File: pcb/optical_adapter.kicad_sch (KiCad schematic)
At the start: 17 parts, among them J1 Conn_01x06_Pin, Q1 BC847, Q2 BC847, Q3 BC857, Q4 BC817, U1 LM1117MP-3.3

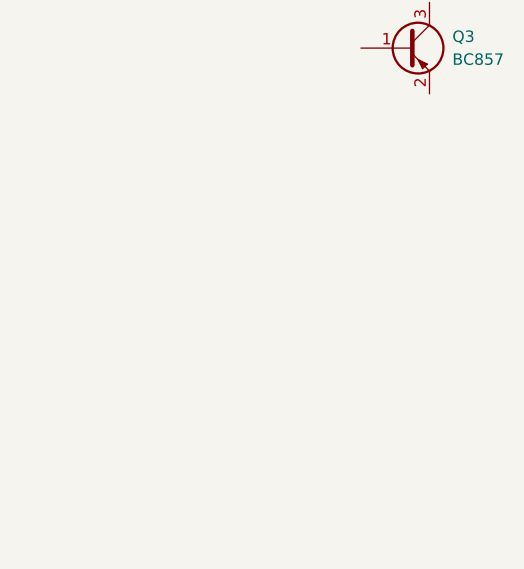
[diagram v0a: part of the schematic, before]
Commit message: Add PCB coil footprint
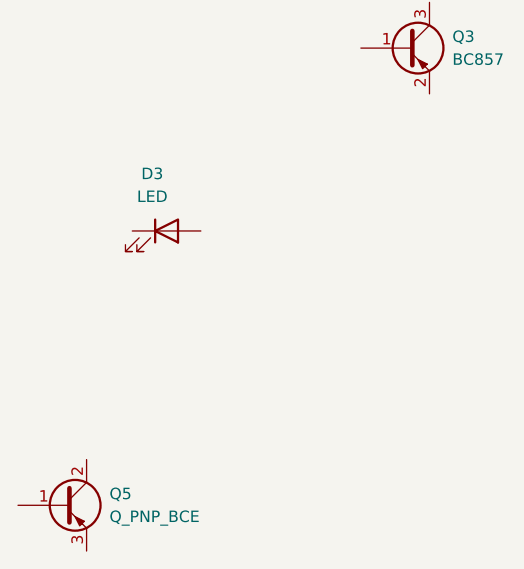
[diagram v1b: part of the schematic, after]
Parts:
- added D3: LED, symbol Device:LED
- added Q5: Q_PNP_BCE, symbol Device:Q_PNP_BCE
- L1: footprint (none) -> footprints:26_turn_16_dia_5_mil
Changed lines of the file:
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@@
 			)
 		)
-		(property "Footprint" ""
+		(property "Footprint" "footprints:26_turn_16_dia_5_mil"
 			(at 106.68 80.01 0)
 			(effects
@@
 			)
 		)
+		(property "LCSC" ""
+			(at 106.68 80.01 0)
+			(effects
+				(font
+					(size 1.27 1.27)
+				)
+				(hide yes)
+			)
+		)
 		(pin "2"
 		)
@@
 	)
 	(symbol
+		(lib_id "Device:LED")
+		(at 50.8 64.77 0)
+		(unit 1)
+		(exclude_from_sim no)
+		(in_bom yes)
+		(on_board yes)
+		(dnp no)
+		(fields_autoplaced yes)
+		(property "Reference" "D3"
+			(at 49.2125 58.42 0)
+			(effects
+				(font
+					(size 1.27 1.27)
+				)
+			)
+		)
+		(property "Value" "LED"
+			(at 49.2125 60.96 0)
+			(effects
+				(font
+					(size 1.27 1.27)
+				)
+			)
+		)
+		(property "Footprint" ""
+			(at 50.8 64.77 0)
+			(effects
+				(font
+					(size 1.27 1.27)
+				)
+				(hide yes)
+			)
+		)
+		(property "Datasheet" "~"
+			(at 50.8 64.77 0)
+			(effects
+				(font
+					(size 1.27 1.27)
+				)
+				(hide yes)
+			)
+		)
+		(property "Description" "Light emitting diode"
+			(at 50.8 64.77 0)
+			(effects
+				(font
+					(size 1.27 1.27)
+				)
+				(hide yes)
+			)
+		)
+		(pin "2"
+		)
+		(pin "1"
+		)
+		(instances
+			(project ""
+				(path "/eed9174b-005f-42ed-94b9-b0e600055621"
+					(reference "D3")
+					(unit 1)
+				)
+			)
+		)
+	)
+	(symbol
 		(lib_id "Jumper:SolderJumper_3_Bridged12")
 		(at 162.56 25.4 0)
@@
 					(unit 1)
 				)
+			)
+		)
+	)
+	(symbol
+		(lib_id "Device:Q_PNP_BCE")
+		(at 39.37 95.25 0)
+		(unit 1)
+		(exclude_from_sim no)
+		(in_bom yes)
+		(on_board yes)
+		(dnp no)
+		(fields_autoplaced yes)
+		(property "Reference" "Q5"
+			(at 44.45 93.9799 0)
+			(effects
+				(font
+					(size 1.27 1.27)
+				)
+				(justify left)
+			)
+		)
+		(property "Value" "Q_PNP_BCE"
+			(at 44.45 96.5199 0)
+			(effects
+				(font
+					(size 1.27 1.27)
+				)
+				(justify left)
+			)
+		)
+		(property "Footprint" ""
+			(at 44.45 92.71 0)
+			(effects
+				(font
+					(size 1.27 1.27)
+				)
+				(hide yes)
+			)
+		)
+		(property "Datasheet" "~"
+			(at 39.37 95.25 0)
+			(effects
+				(font
+					(size 1.27 1.27)
+				)
+				(hide yes)
+			)
+		)
+		(property "Description" "PNP transistor, base/collector/emitter"
+			(at 39.37 95.25 0)
+			(effects
+				(font
+					(size 1.27 1.27)
+				)
+				(hide yes)
+			)
+		)
+		(pin "2"
+		)
+		(pin "1"
+		)
+		(pin "3"
+		)
+		(instances
+			(project ""
+				(path "/eed9174b-005f-42ed-94b9-b0e600055621"
+					(reference "Q5")
+					(unit 1)
+				)

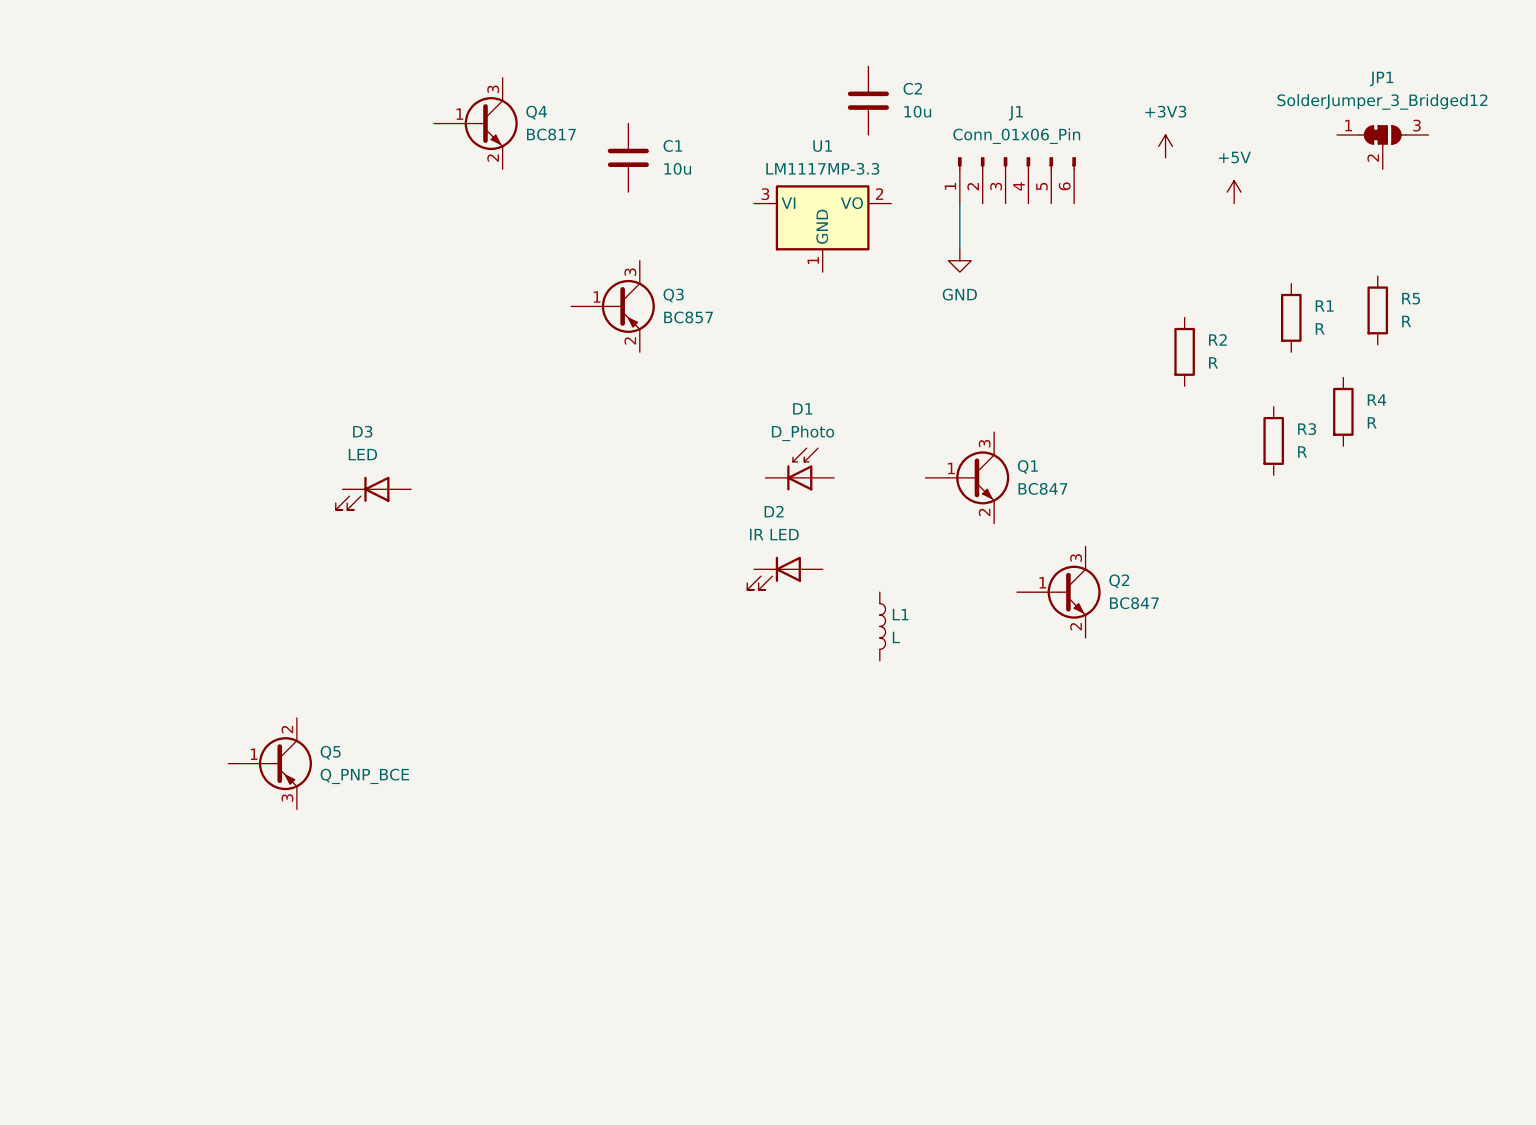
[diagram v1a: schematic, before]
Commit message: Add power supply circuit
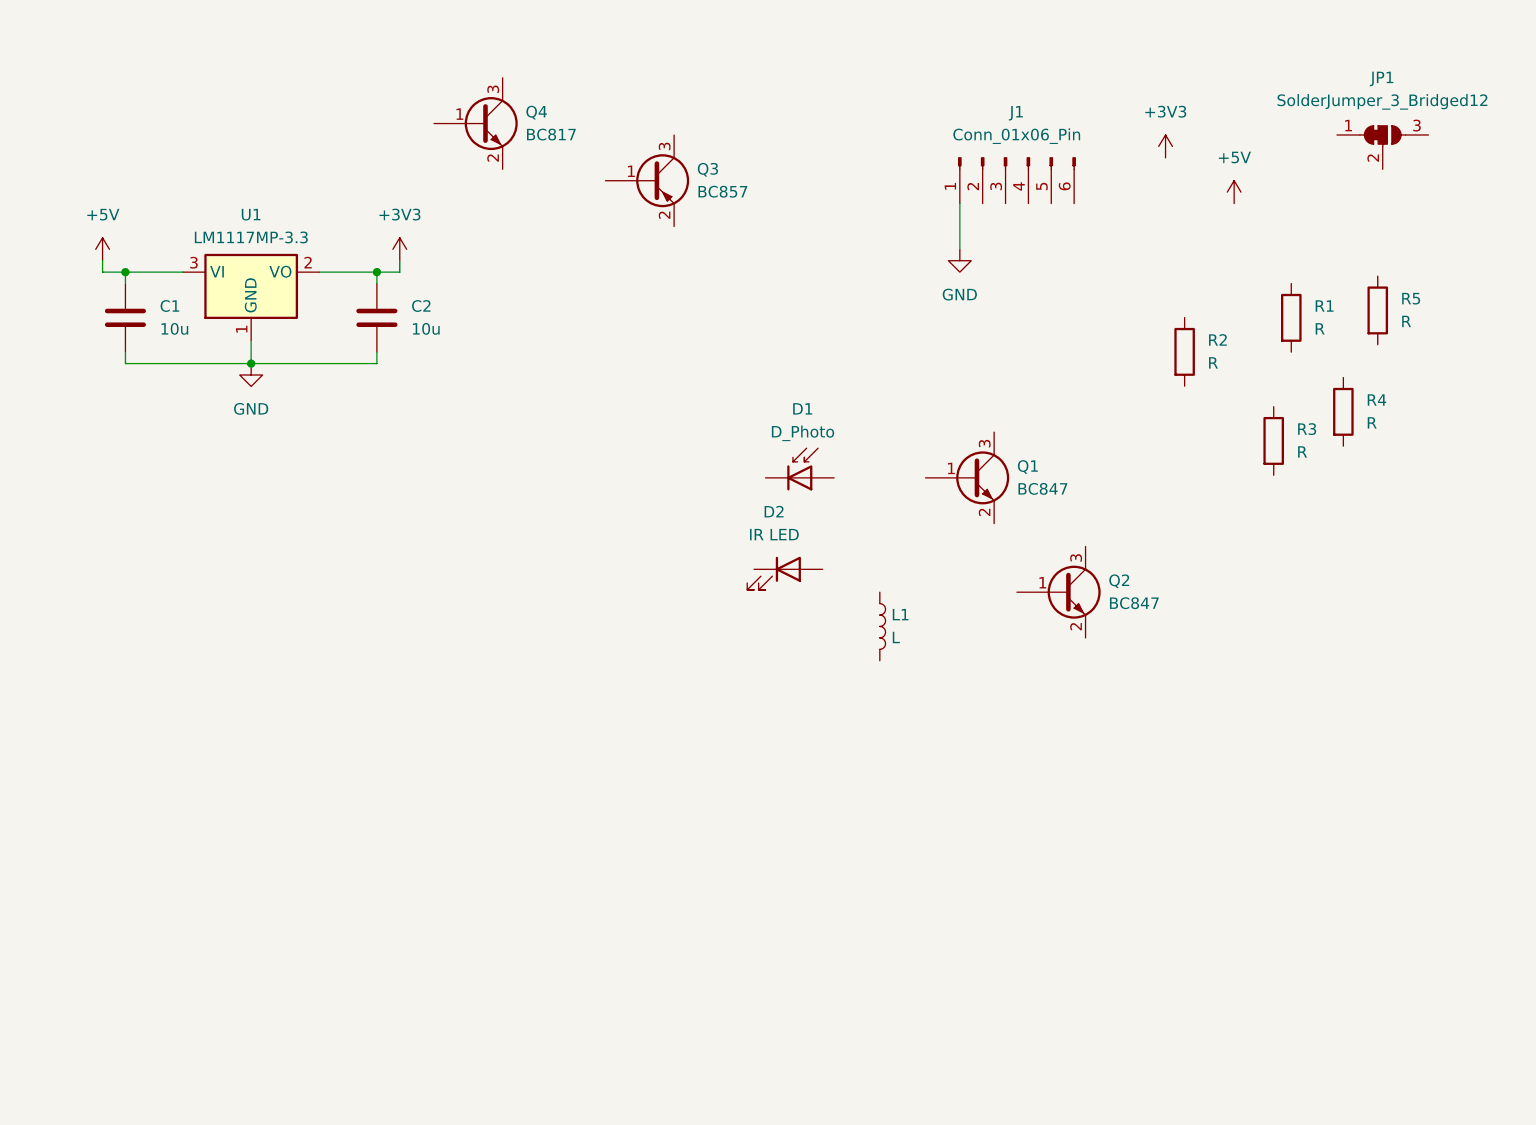
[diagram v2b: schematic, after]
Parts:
- removed D3: LED, symbol Device:LED
- removed Q5: Q_PNP_BCE, symbol Device:Q_PNP_BCE
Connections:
- net +3V3: now also C2.1, U1.2 (VO)
- net +5V: now also C1.1, U1.3 (VI)
- net GND: now also C1.2, C2.2, U1.1 (GND)
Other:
- moved on the sheet: C1, C2, Q3, U1

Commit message: Add IR RX/TX circuit
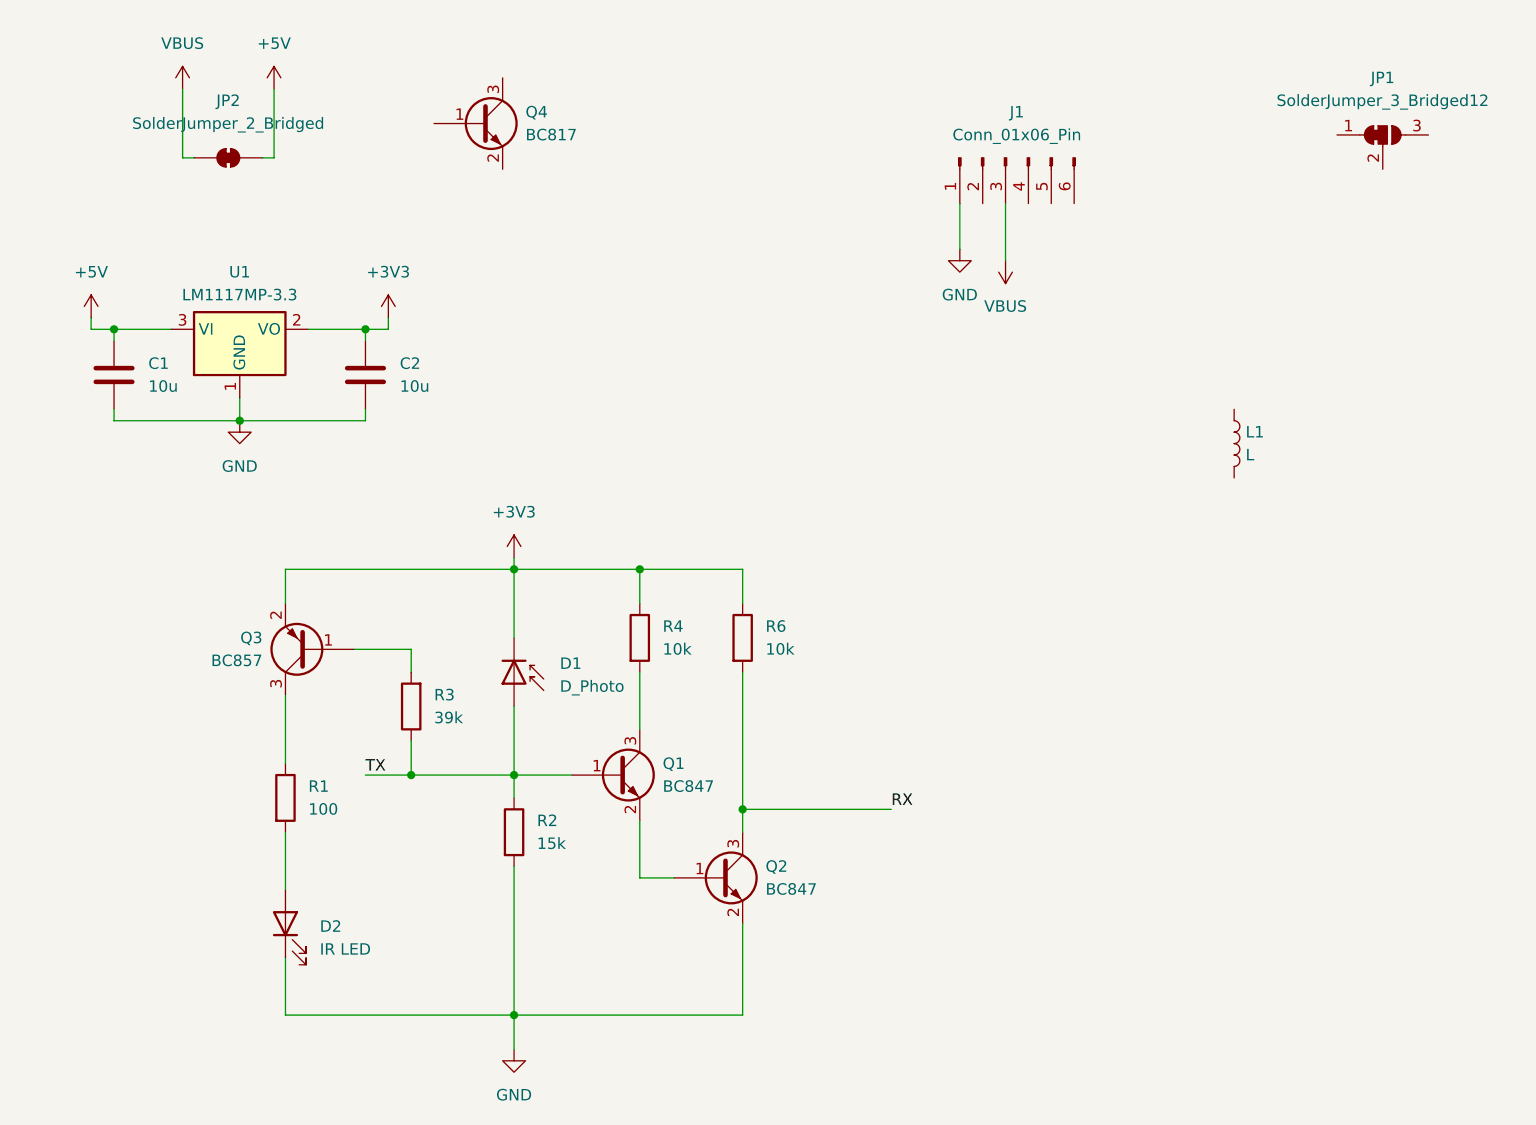
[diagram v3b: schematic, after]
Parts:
- removed R5: R, Resistor_SMD:R_1206_3216Metric_Pad1.30x1.75mm_HandSolder, symbol Device:R
- added JP2: SolderJumper_2_Bridged, Jumper:SolderJumper-2_P1.3mm_Open_TrianglePad1.0x1.5mm, symbol Jumper:SolderJumper_2_Bridged
- added R6: 10k, Resistor_SMD:R_1206_3216Metric_Pad1.30x1.75mm_HandSolder, symbol Device:R
- R1: value R -> 100
- R2: value R -> 15k
- R3: value R -> 39k
- R4: value R -> 10k
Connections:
- net +3V3: now also D1.1 (K), Q3.2 (E), R4.1, R6.1
- net +5V: now also JP2.2 (B)
- net GND: now also D2.1 (K), Q2.2 (E), R2.2
- net VBUS: now reaches J1.3 (Pin_3)
- net VBUS: now also JP2.1 (A)
- net at Q2.1 (B): now also Q1.2 (E)
- net RX: now reaches Q2.3 (C)
- net RX: now also R6.2
- net TX: now reaches D1.2 (A)
- net TX: now also Q1.1 (B), R2.1, R3.1
- net at R4.2: now also Q1.3 (C)
- net at R1.1: now also Q3.3 (C)
- net at R1.2: now also D2.2 (A)
- net at R3.2: now also Q3.1 (B)
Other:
- moved on the sheet: C1, C2, D1, D2, L1, Q1, Q2, Q3, R1, R2, R3, R4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

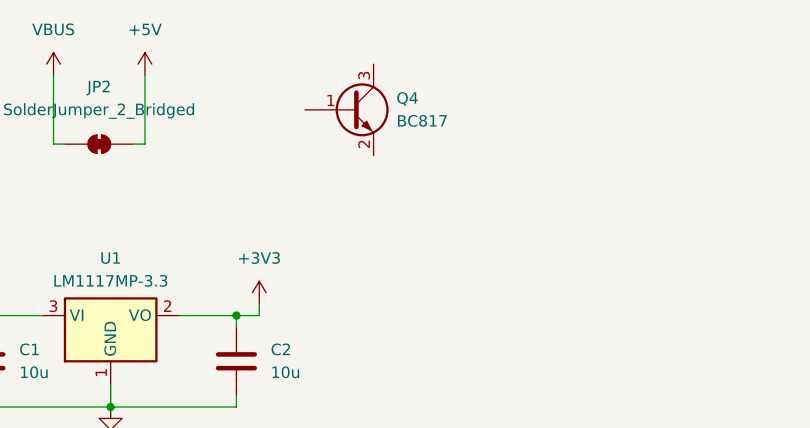
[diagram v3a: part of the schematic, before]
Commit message: Rough PCB component layout
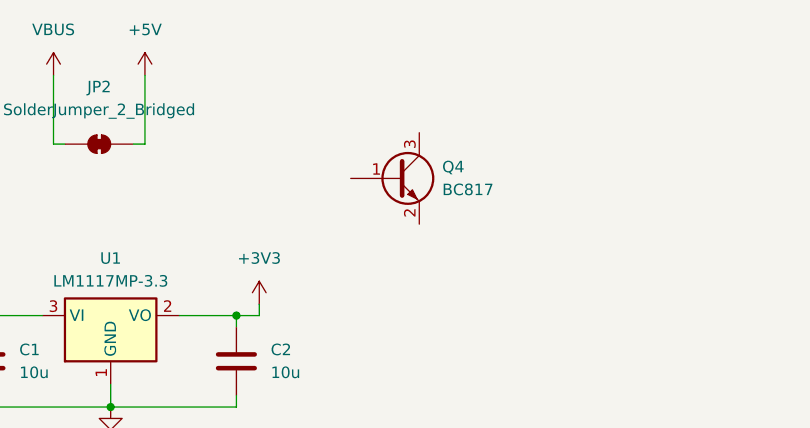
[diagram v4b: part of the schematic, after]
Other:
- moved on the sheet: Q4
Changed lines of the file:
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@@
 	(symbol
 		(lib_id "Transistor_BJT:BC817")
-		(at 62.23 24.13 0)
+		(at 67.31 31.75 0)
 		(unit 1)
 		(exclude_from_sim no)
@@
 		(fields_autoplaced yes)
 		(property "Reference" "Q4"
-			(at 67.31 22.8599 0)
+			(at 72.39 30.4799 0)
 			(effects
 				(font
@@
 		)
 		(property "Value" "BC817"
-			(at 67.31 25.3999 0)
+			(at 72.39 33.0199 0)
 			(effects
 				(font
@@
 		)
 		(property "Footprint" "Package_TO_SOT_SMD:SOT-23"
-			(at 67.31 26.035 0)
+			(at 72.39 33.655 0)
 			(effects
 				(font
@@
 		)
 		(property "Datasheet" "https://www.onsemi.com/pub/Collateral/BC818-D.pdf"
-			(at 62.23 24.13 0)
+			(at 67.31 31.75 0)
 			(effects
 				(font
@@
 		)
 		(property "Description" "0.8A Ic, 45V Vce, NPN Transistor, SOT-23"
-			(at 62.23 24.13 0)
+			(at 67.31 31.75 0)
 			(effects
 				(font
